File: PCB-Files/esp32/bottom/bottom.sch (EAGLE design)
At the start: 19 parts, among them X2 ESP32_WROOM32_SKINNY

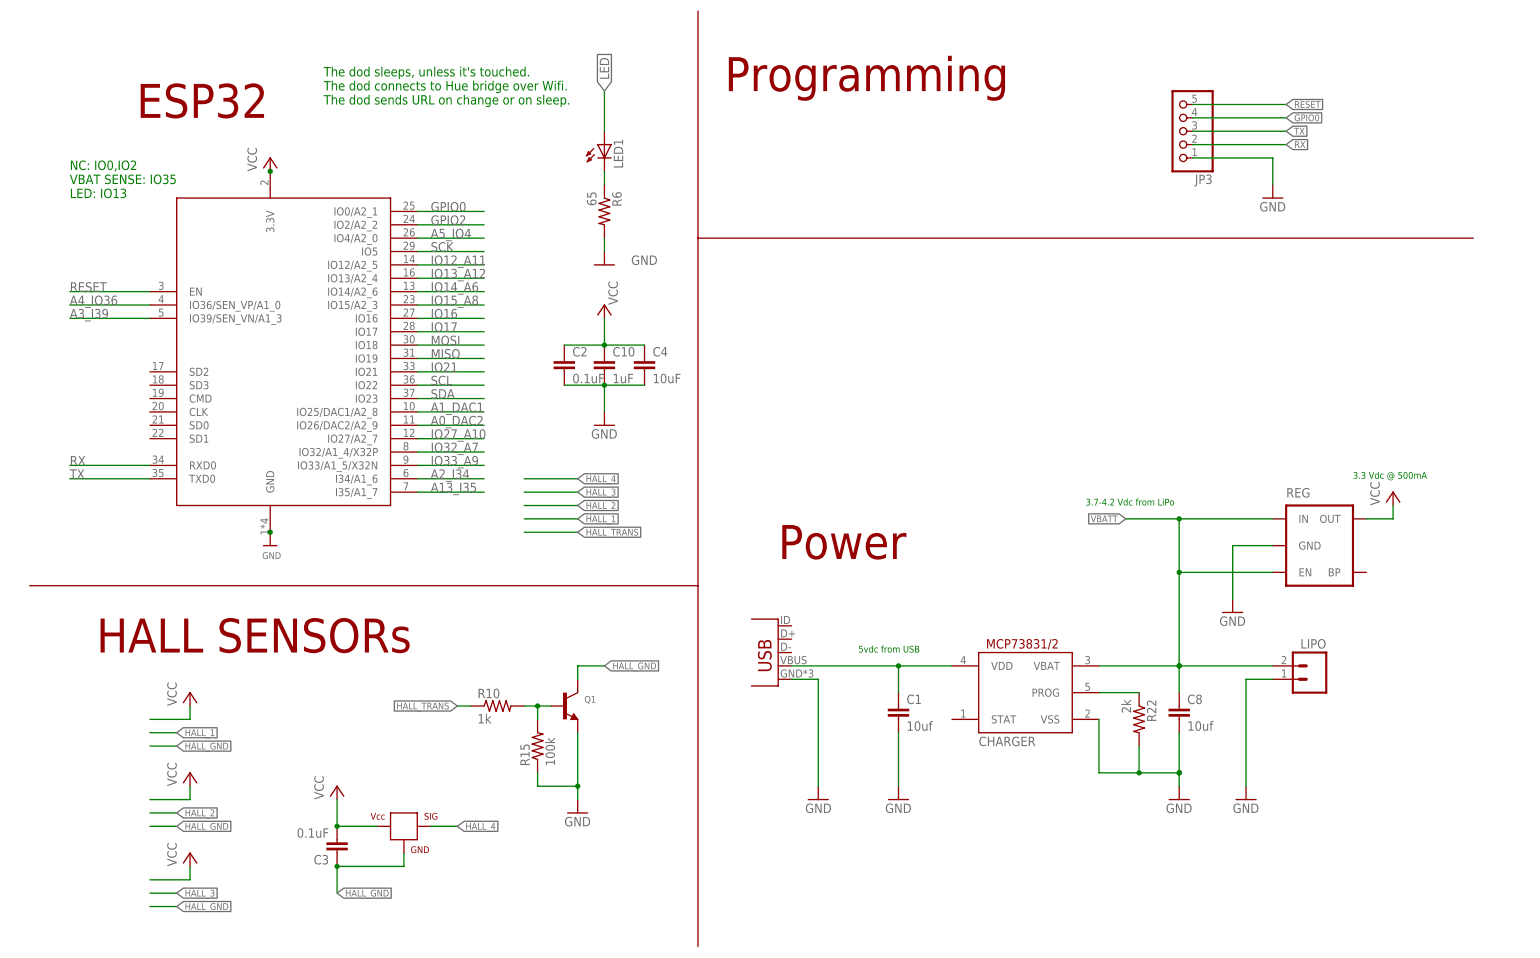
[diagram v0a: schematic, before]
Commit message: initial files for 4-sided PCBs; no routing done yet
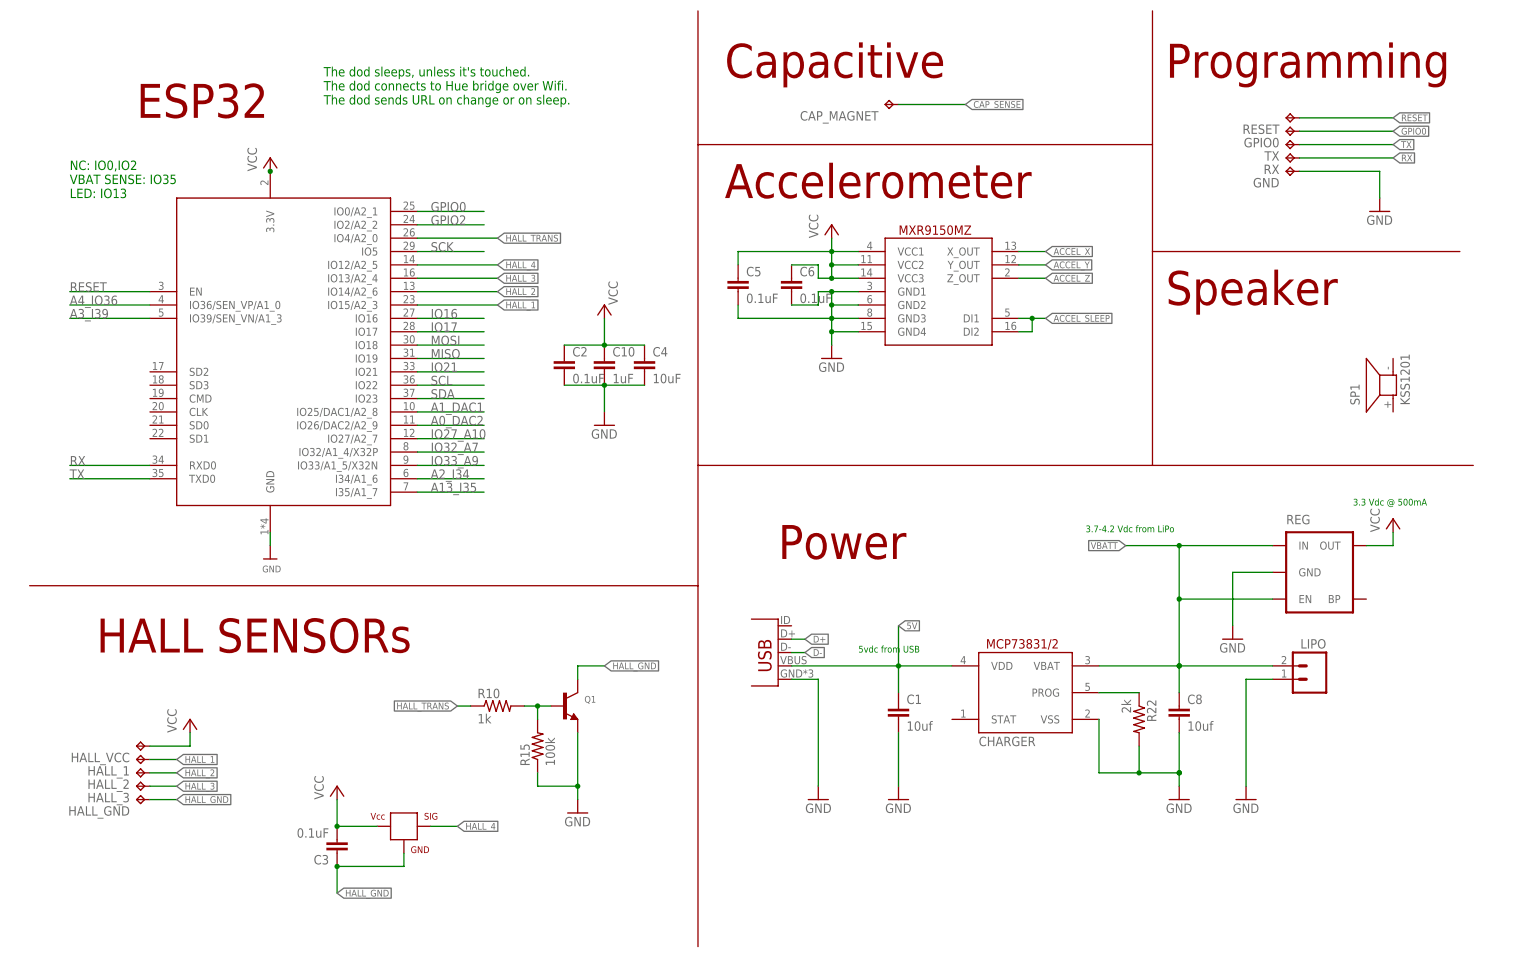
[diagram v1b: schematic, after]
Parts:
- removed JP3: (no value), pinhead:PINHD-1X55X2MM
- removed LED1: (no value), adafruit:LEDCHIPLED_0603
- removed R6: 65, SparkFun-Resistors:RESISTOR0805-RES
- added C5, C6: 0.1uF, SparkFun:CAP0402-CAP
- added CAP_MAGNET: TPTP10R, testpad:TPTP10R
- added GND: TPTP13SQ, testpad:TPTP13SQ
- added GPIO0, RESET, RX, TX: TPTP13R, testpad:TPTP13R
- added HALL_1, HALL_2, HALL_3, HALL_GND, HALL_VCC: TPTP20SQ, testpad:TPTP20SQ
- added SP1: KSS1201, buzzer:KSS1201
- added U$1: ACCELEROMETER_MXR9150MZ, Andy_Sigler_2019:ACCELEROMETER_MXR9150MZ
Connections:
- removed net A5_IO4: X2.IO4/A2_0
- removed net IO12_A11: X2.IO12/A2_5
- removed net IO13_A12: X2.IO13/A2_4
- removed net IO14_A6: X2.IO14/A2_6
- removed net IO15_A8: X2.IO15/A2_3
- removed net LED: LED1.A
- removed net N$1: LED1.C, R6.1
- new net ACCEL_SLEEP: U$1.DI1, U$1.DI2
- new net ACCEL_X: U$1.X_OUT
- new net ACCEL_Y: U$1.Y_OUT
- new net ACCEL_Z: U$1.Z_OUT
- new net CAP_SENSE: CAP_MAGNET.TP
- new net D+: JP1.D+
- new net D-: JP1.D-
- new net HALL_1: HALL_1.TP, X2.IO15/A2_3
- new net HALL_2: HALL_2.TP, X2.IO14/A2_6
- new net HALL_3: HALL_3.TP, X2.IO13/A2_4
- net GND: now also C5.2, C6.2, GND.TP, U$1.GND1, U$1.GND2, U$1.GND3, U$1.GND4; no longer JP3.1, R6.2
- net GPIO0: now also GPIO0.TP; no longer JP3.4
- net HALL_4: now also X2.IO12/A2_5
- net HALL_GND: now also HALL_GND.TP
- net HALL_TRANS: now also X2.IO4/A2_0
- net RESET: now also RESET.TP; no longer JP3.5
- net RX: now also RX.TP; no longer JP3.2
- net TX: now also TX.TP; no longer JP3.3
- net VCC: now also C5.1, C6.1, HALL_VCC.TP, U$1.VCC1, U$1.VCC2, U$1.VCC3
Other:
- note added: "A5_IO4"
- note added: "Accelerometer"
- note added: "Capacitive"
- note added: "IO12_A11"
- note added: "IO13_A12"
- note added: "IO14_A6"
- note added: "IO15_A8"
- note added: "Speaker"
- moved on the sheet: REG

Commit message: main PCB ready to mill for beta
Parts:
- removed HALL_1, HALL_2, HALL_3, HALL_GND, HALL_VCC: TPTP20SQ, testpad:TPTP20SQ
- added C7: 0.1uF, SparkFun:CAP0402-CAP
- added C9: 10uF, SparkFun:CAP0402-CAP
- added R1: 10M, SparkFun-Passives:RESISTOR0402-RES
- added TP1, TP10, TP11, TP12, TP2, TP3, TP4, TP5, TP6, TP7, TP8, TP9: TPSQTP10SQ, testpad:TPSQTP10SQ
- C10: value 1uF -> 10uF
- C2: value 0.1uF -> 10uf
- C4: value 10uF -> 0.1uF
- HALL: value HALLEFFECT-A1326 -> A1304
- LIPO: device SparkFun:M02 -> adafruit:JST_2PIN-THM
- R15: value 100k -> 10M
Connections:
- removed net A13_I35: X2.I35/A1_7
- removed net A1_DAC1: X2.IO25/DAC1/A2_8
- removed net A2_I34: X2.I34/A1_6
- removed net A3_I39: X2.IO39/SEN_VN/A1_3
- removed net A4_IO36: X2.IO36/SEN_VP/A1_0
- removed net CAP_SENSE: CAP_MAGNET.TP
- removed net IO32_A7: X2.IO32/A1_4/X32P
- removed net IO33_A9: X2.IO33/A1_5/X32N
- removed net SCK: X2.IO5
- removed net SDA: X2.IO23
- new net IO13_A12: X2.IO13/A2_4
- new net IO14_A6: X2.IO14/A2_6
- new net IO15_A8: X2.IO15/A2_3
- new net SPEAKER: SP1.1, X2.IO23
- new net TOUCH: CAP_MAGNET.TP, TP11.TP, TP12.TP, X2.IO4/A2_0
- net ACCEL_SLEEP: now also R1.1, X2.IO5
- net ACCEL_X: now also X2.IO36/SEN_VP/A1_0
- net ACCEL_Y: now also X2.IO39/SEN_VN/A1_3
- net ACCEL_Z: now also X2.I34/A1_6
- net GND: now also C7.2, C9.2, SP1.2
- net HALL_1: now also TP10.TP, TP3.TP, X2.I35/A1_7; no longer HALL_1.TP, X2.IO15/A2_3
- net HALL_2: now also TP4.TP, TP9.TP, X2.IO32/A1_4/X32P; no longer HALL_2.TP, X2.IO14/A2_6
- net HALL_3: now also TP5.TP, TP8.TP, X2.IO33/A1_5/X32N; no longer HALL_3.TP, X2.IO13/A2_4
- net HALL_4: now also X2.IO25/DAC1/A2_8; no longer X2.IO12/A2_5
- net HALL_GND: now also TP6.TP, TP7.TP; no longer HALL_GND.TP
- net HALL_TRANS: now also X2.IO12/A2_5; no longer X2.IO4/A2_0
- net VCC: now also C7.1, C9.1, R1.2, TP1.TP, TP2.TP; no longer HALL_VCC.TP
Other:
- note added: "A13_135"
- note added: "A1_DAC1"
- note added: "A2_134"
- note added: "A3_I39"
- note added: "A4_IO36"
- note added: "IO27_A10"
- note added: "IO32_A7"
- note added: "IO33_A9"
- note added: "SCK/IO5"
- note added: "SDA/IO23"
- moved on the sheet: LIPO
